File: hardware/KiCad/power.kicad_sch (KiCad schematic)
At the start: 24 parts, among them U4 SCT2A25STER, U5 SY8120B1ABC

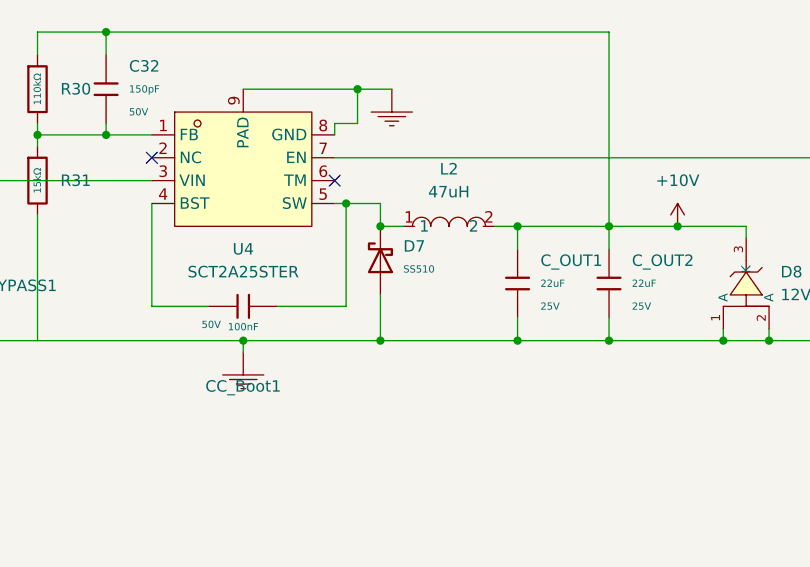
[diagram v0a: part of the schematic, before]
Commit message: Vendor easyeda2kicad component library; rename project files; fix stale part data
Vendors the 16 easyeda2kicad:* parts (symbols/footprints/3D models) that
were referenced but never committed, registers them in sym-lib-table and
a new fp-lib-table, and adds the EASYEDA2KICAD project text variable so
existing 3D-model paths resolve.

Also corrects BSC030N08NS5's stale metadata (was pointing at an ElecSuper
clone, C49108769, instead of the genuine Infineon part, C501507) and
swaps its footprint to the freshly-fetched one, and fixes STANDARDS.md's
Hardware Universe table (stale reference designators, stale MOSFET/
CC6937 LCSC numbers, ~13 previously undocumented parts, wrong library
path).

Renames the auto-generated project/sheet filenames to something legible:
ProPrj_STM32 MPPT_2024-07-25_15-40-35_2026-05-30.* -> openMPPT_v1.3.*,
and the numbered "N_Name Stuff.kicad_sch" sheets -> mcu/buck_boost/
connectors.kicad_sch. Verified via kicad-cli ERC/DRC before and after -
same violation counts, no structural breakage.

Co-Authored-By: Claude Sonnet 5 <noreply@anthropic.com>
Claude-Session: https://claude.ai/code/session_01FKwww6crXDCSrRUFRETJEs
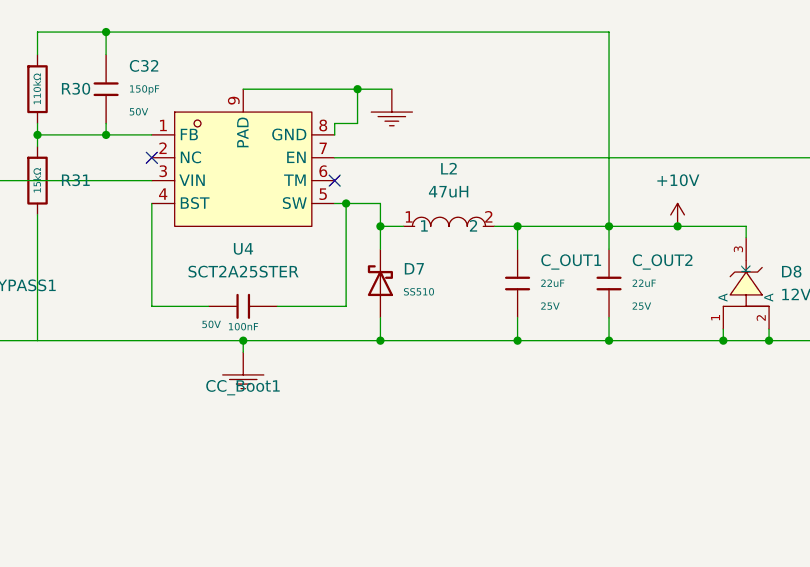
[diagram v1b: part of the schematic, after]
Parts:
- D7: LCSC C18199171 -> C7420368
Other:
- moved on the sheet: D7

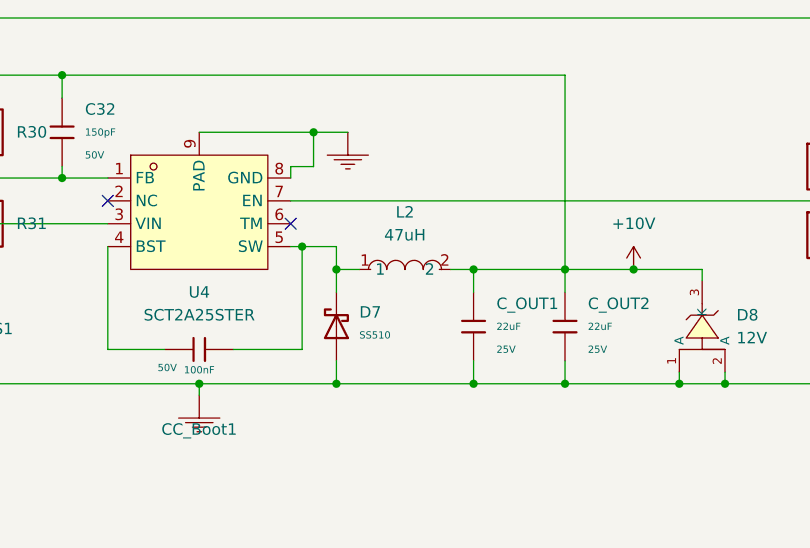
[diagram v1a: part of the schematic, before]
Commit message: fix: upsize L2 aux inductor for fault-current headroom
Replaces APS0650M470A (47uH, Isat 2.62A, DCR 227mOhm) with GXDR1207-470MT
(FAUKU, C52196367, $0.207, 11735 in stock) for L2, the SCT2A25 10V rail's
inductor. Same 47uH, but Isat now matches SCT2A25's own 4A peak current
limit exactly instead of saturating well below it, and DCR drops to
90mOhm. The original part was sized for the baseline gate-driver/logic
load (~150-500mA), not for a heavier load (e.g. a fan) that might get
added to the 10V rail - same underlying reasoning as why D7 stays SS510
instead of SS210. Applied to both the schematic and PCB (package grew
from 7.7x6.6mm to 12.5x12.5mm SMD).

Co-Authored-By: Claude Sonnet 5 <noreply@anthropic.com>
Claude-Session: https://claude.ai/code/session_01FKwww6crXDCSrRUFRETJEs
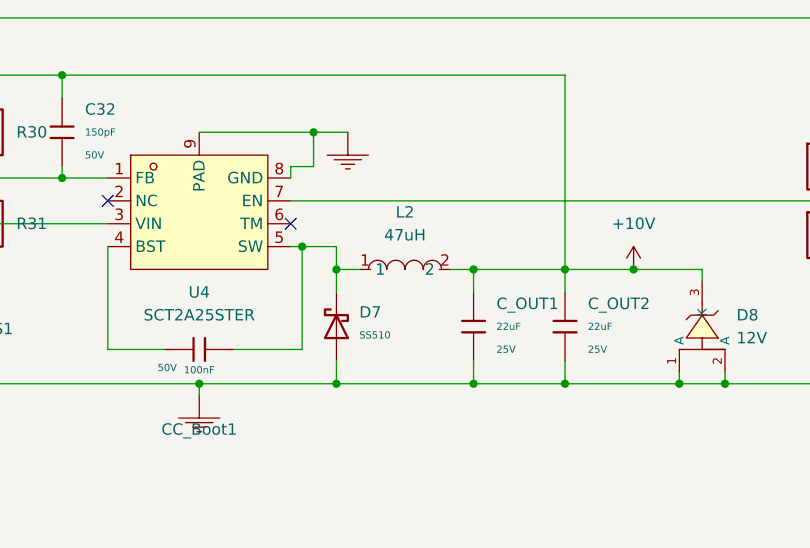
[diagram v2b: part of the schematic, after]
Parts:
- L2: footprint easyeda2kicad:IND-SMD_L7.7-W6.6_APS07A30M220 -> easyeda2kicad:IND-SMD_L12.5-W12.5-1; symbol easyeda2kicad:APS0650M470A -> easyeda2kicad:GXDR1207-470MT; LCSC Part C47327224 -> C52196367; MPN APS0650M470A -> GXDR1207-470MT; Manufacturer Coilank(驰兴电感) -> FAUKU(高芯电子)
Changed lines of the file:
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@@
 	)
 	(symbol
-		(lib_id "easyeda2kicad:APS0650M470A")
+		(lib_id "easyeda2kicad:GXDR1207-470MT")
 		(at 119.38 66.04 0)
 		(unit 1)
@@
 			)
 		)
-		(property "Footprint" "easyeda2kicad:IND-SMD_L7.7-W6.6_APS07A30M220"
+		(property "Footprint" "easyeda2kicad:IND-SMD_L12.5-W12.5-1"
 			(at 119.38 73.66 0)
 			(hide yes)
@@
 			)
 		)
-		(property "Datasheet" "https://www.lcsc.com/datasheet/C47327224.pdf"
+		(property "Datasheet" "https://www.lcsc.com/datasheet/C52196367.pdf"
 			(at 119.38 76.2 0)
 			(hide yes)
@@
 			)
 		)
-		(property "Manufacturer" "Coilank(驰兴电感)"
+		(property "Manufacturer" "FAUKU(高芯电子)"
 			(at 119.38 78.74 0)
 			(hide yes)
@@
 			)
 		)
-		(property "MPN" "APS0650M470A"
+		(property "MPN" "GXDR1207-470MT"
 			(at 119.38 81.28 0)
 			(hide yes)
@@
 			)
 		)
-		(property "LCSC Part" "C47327224"
+		(property "LCSC Part" "C52196367"
 			(at 119.38 83.82 0)
 			(hide yes)
